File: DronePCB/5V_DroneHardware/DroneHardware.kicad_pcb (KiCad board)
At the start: 6 copper layers, 36.1 x 36 mm, 40 parts, among them J301 USB_B_Micro, J302 BATTERY, J303 SWD_CONN, SW1 SW_SPDT, U1 STM32F405RGT6, U301 USBLC6-2SC6, U303 MPU-6000, Y1 16MHz

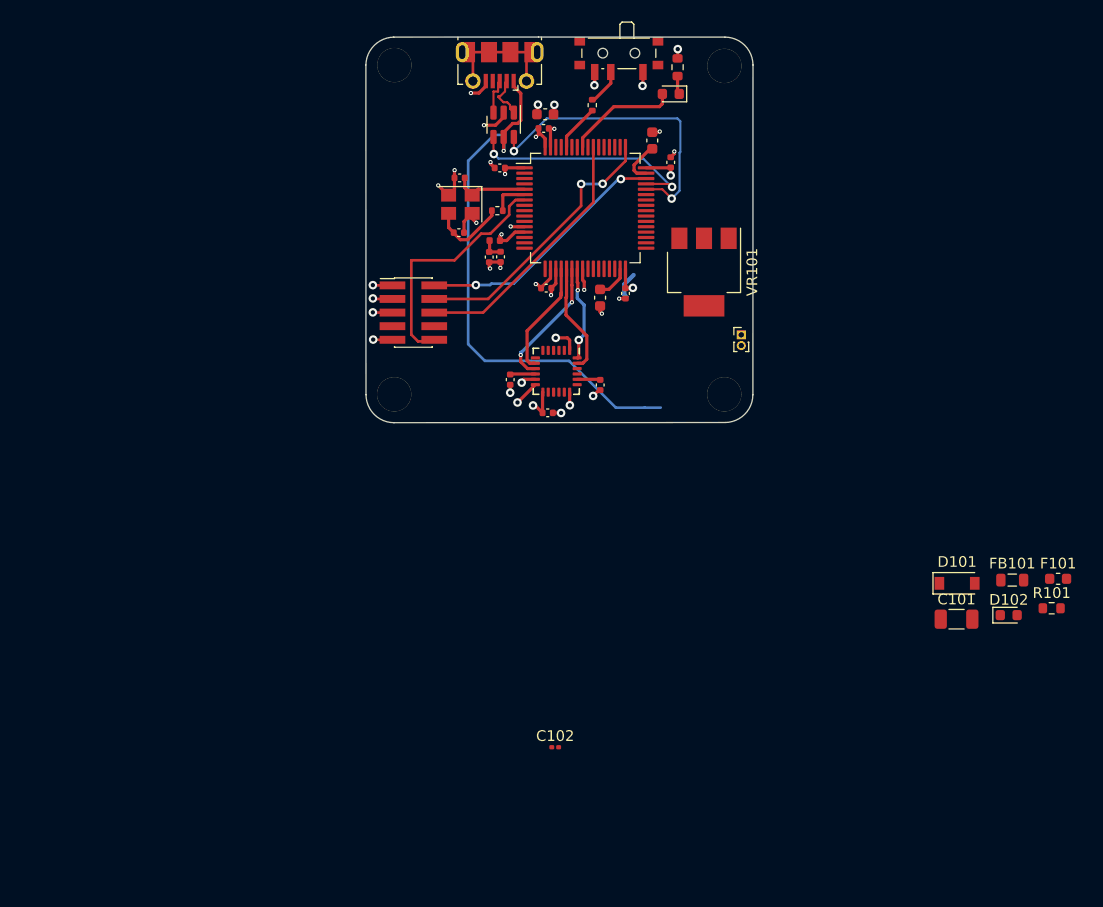
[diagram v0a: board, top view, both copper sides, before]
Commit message: Creazione della scheda con il convertitore da 5V a 3.3V
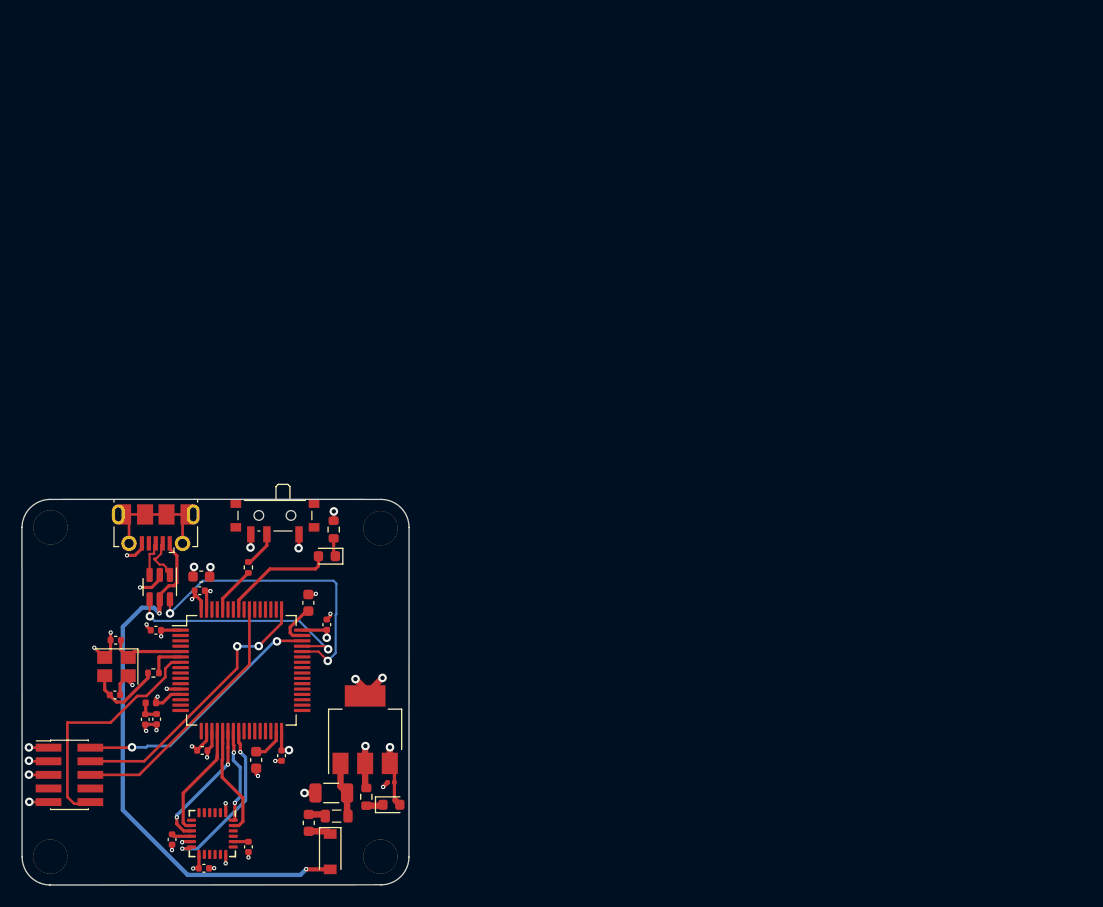
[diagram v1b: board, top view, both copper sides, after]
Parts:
- removed J302: BATTERY, Connector_PinHeader_1.00mm:PinHeader_1x02_P1.00mm_Vertical
- moved F101 73.6 mm to (154.7, 113.3), turned to 90 degrees
- moved FB101 66.8 mm to (157.3, 112.6)
- moved R101 66.3 mm to (160.1, 110.8), turned to -90 degrees
- moved D101 63.6 mm to (156.7, 116.0), turned to -90 degrees
- moved C101 60.6 mm to (156.8, 110.5), turned to 180 degrees
- moved D102 60.3 mm to (162.4, 111.6)
- moved C317 54.2 mm to (149.1, 115.5)
- moved C8 53.8 mm to (144.8, 106.5)
- moved C2 53.8 mm to (144.7, 90.3)
- moved D1 53.8 mm to (156.4, 88.4)
- moved H303 53.8 mm to (161.4, 85.8)
- moved J301 53.8 mm to (140.4, 85.7)
- moved R2 53.8 mm to (140.2, 99.3)
- moved C1 53.8 mm to (149.8, 107.4)
- moved C10 53.8 mm to (140.5, 103.6)
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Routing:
- net GND: track 39.9 -> 46.6 mm, vias 27 -> 32
- net BUCK_IN: track 0.00 -> 5.21 mm
- net BUCK_VOUT_3V3: track 24.0 -> 28.5 mm, vias 10 -> 11
- net GYRO_INT_EXTI: track 18.9 -> 15.4 mm
- net (no net): track 2.50 -> 0.00 mm
- net Net-(D101-Pad1): track 0.00 -> 2.10 mm
- net Net-(F101-Pad2): track 0.00 -> 1.60 mm
- net Net-(D102-Pad1): track 0.00 -> 1.59 mm
- net Net-(C317-Pad1): track 2.17 -> 1.42 mm
- net +5V: track 51.0 -> 50.9 mm, vias 1 -> 2

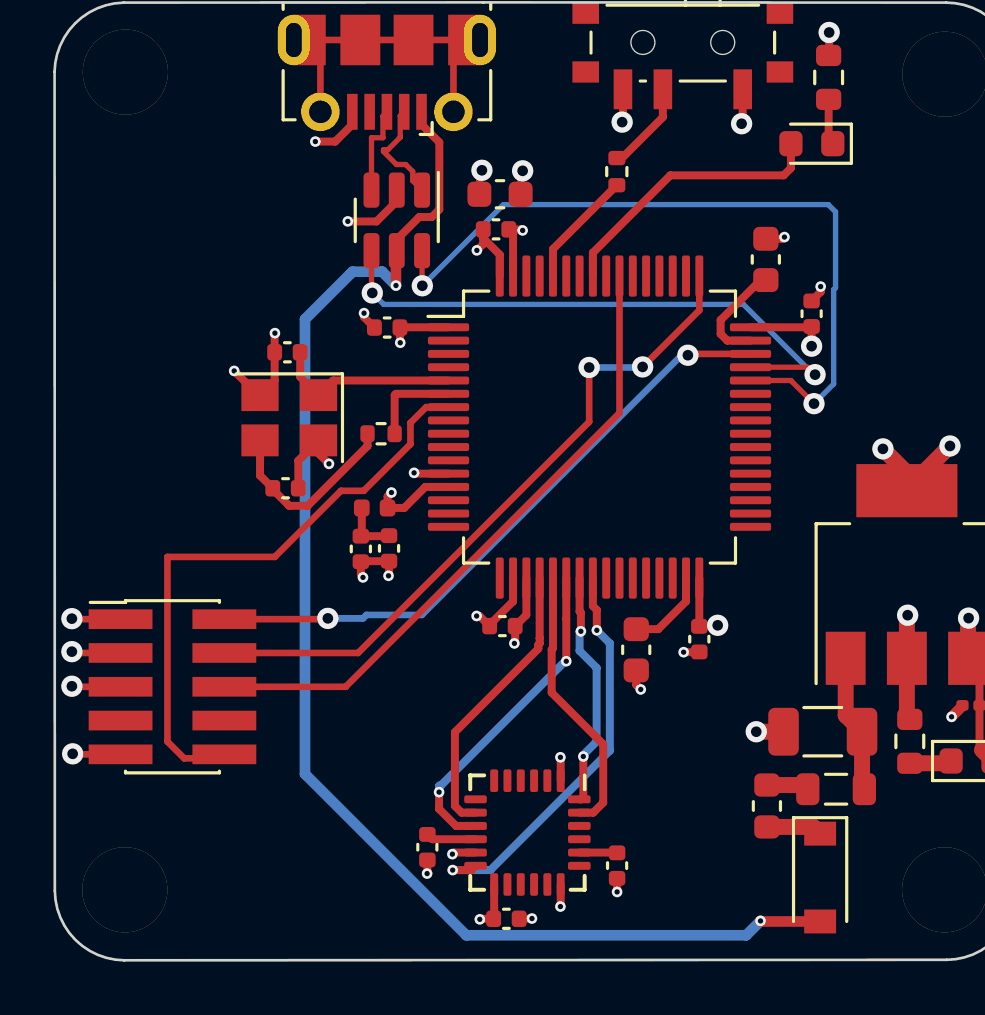
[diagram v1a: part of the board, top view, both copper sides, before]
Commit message: Test per lo spostamento della porta usb
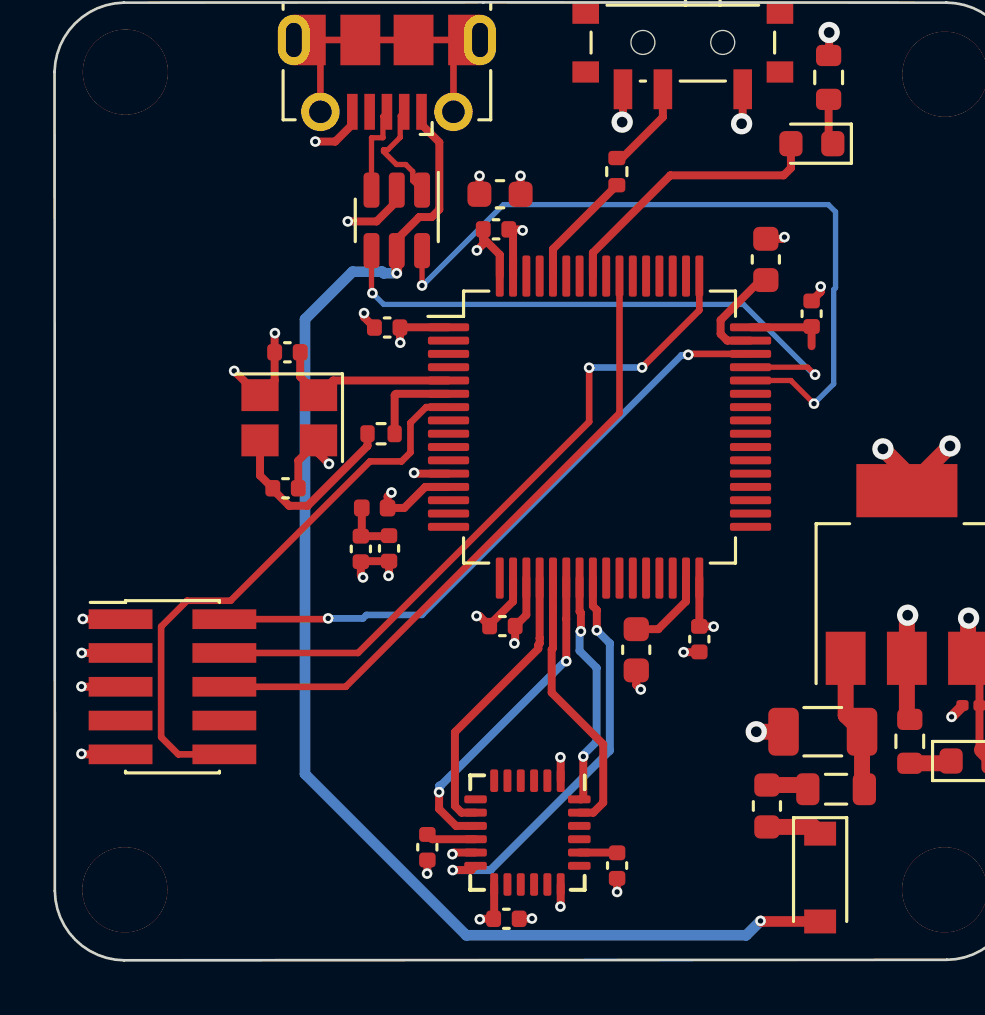
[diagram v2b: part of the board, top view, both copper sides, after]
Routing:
- net GND: track 46.6 -> 45.3 mm
- net NRST: track 22.8 -> 21.7 mm
- net BUCK_VOUT_3V3: track 28.5 -> 27.6 mm, vias 11 -> 10
- net +5V: track 50.9 -> 50.3 mm

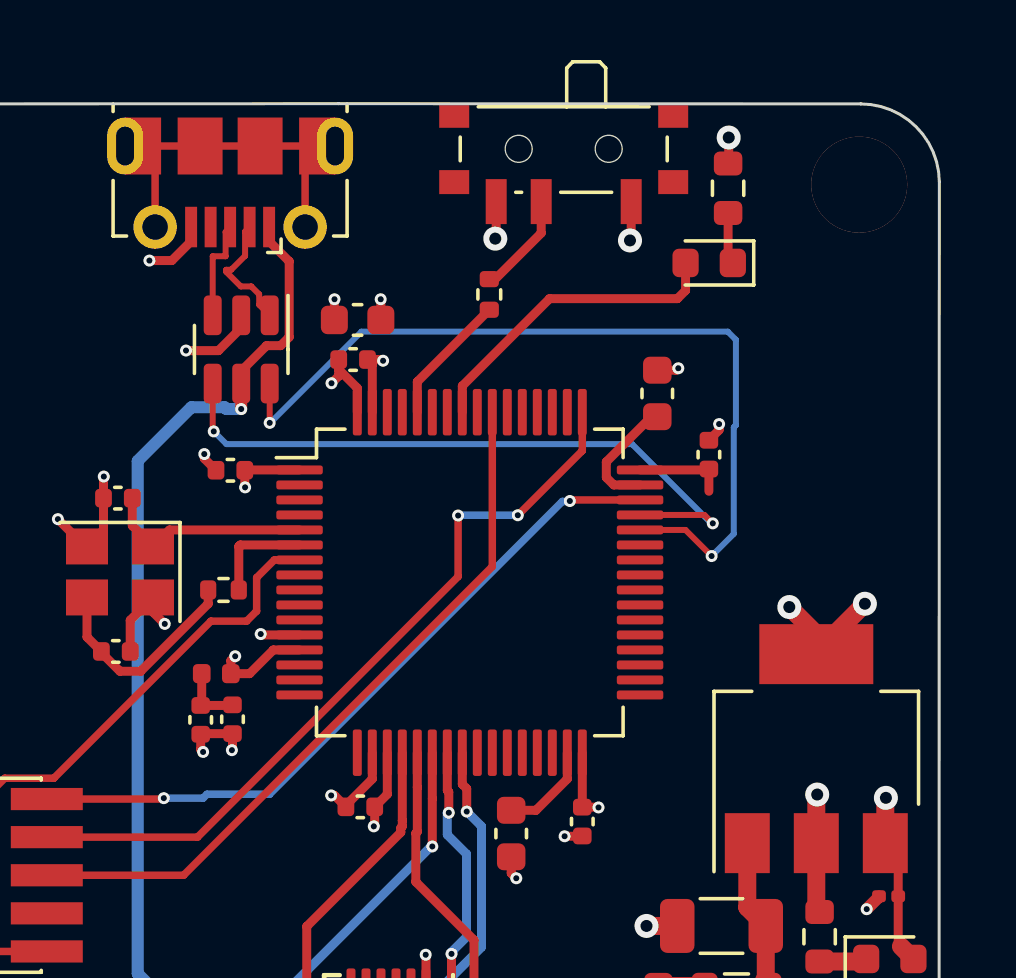
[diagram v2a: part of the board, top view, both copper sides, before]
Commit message: Collegamento di USB con resistenze da 22Ohm
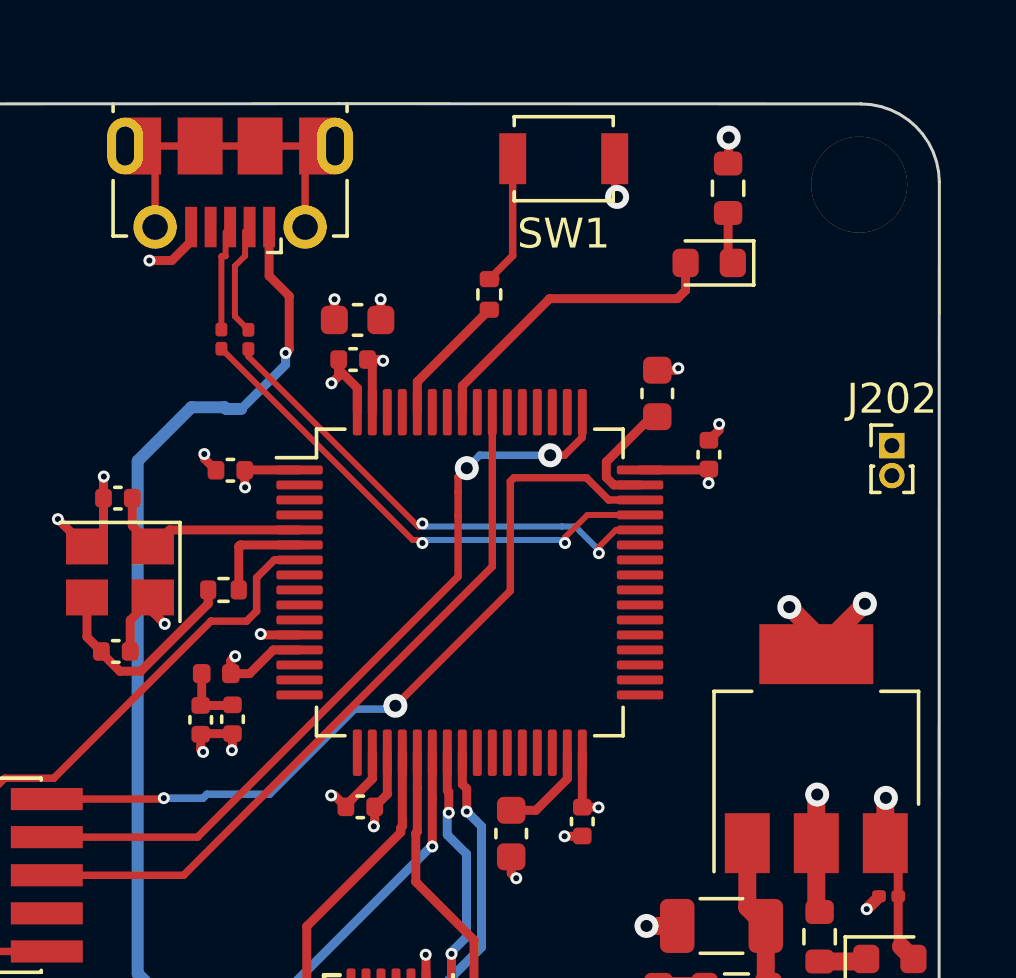
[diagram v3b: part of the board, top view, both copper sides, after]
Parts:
- removed U301: USBLC6-2SC6, Package_TO_SOT_SMD:SOT-23-6
- added J202: BATTERY, Connector_PinHeader_1.00mm:PinHeader_1x02_P1.00mm_Vertical, F.Cu at (162.5, 94.5)
- added R201: 22, Resistor_SMD:R_0201_0603Metric, F.Cu at (140.1, 90.9)
- added R202: 22, Resistor_SMD:R_0201_0603Metric, F.Cu at (141.0, 90.9)
- SW1: footprint Button_Switch_SMD:SW_SPDT_PCM12 -> Button_Switch_SMD:SW_SPST_B3U-1000P
- renumbered H301 to H201, H302 to H202, H303 to H203, H304 to H204, J301 to J201, J303 to J203
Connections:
- U1 pad 16: unconnected-(U1-Pad16) -> PWM4
- U1 pad 17: unconnected-(U1-Pad17) -> PWM3
- U1 pad 26: unconnected-(U1-Pad26) -> PWM1
- U1 pad 27: unconnected-(U1-Pad27) -> PWM2
- U1 pad 61: unconnected-(U1-Pad61) -> PPM
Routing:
- net USB_D-: track 28.5 -> 16.8 mm
- net USB_D+: track 22.1 -> 17.2 mm
- net GND: track 45.3 -> 41.4 mm, vias 32 -> 30
- net SWDIO: track 23.9 -> 26.7 mm
- net Net-(R1-Pad2): track 3.42 -> 4.53 mm
- net BUCK_VOUT_3V3: track 27.6 -> 27.4 mm, vias 10 -> 11
